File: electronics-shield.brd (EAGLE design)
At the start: 85 x 56 mm, 76 parts, among them IC1 LINEAR_MCP1703CB, J2 MICRO_USB, Q1 8 MHz, Q2 USER-SUBMITTED_MOSFET-PCHANNE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, Q3 ON-SEMICONDUCTOR---NTZD3154NT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, Q4 ON-SEMICONDUCTOR---NTZD3154NT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, U1 TLE9201SG, U2 TLE9201SG, U3 TLE9201SG, U4 TLE9201SG, U5 STM32F0XX8T, U8 EEPROM-I2C

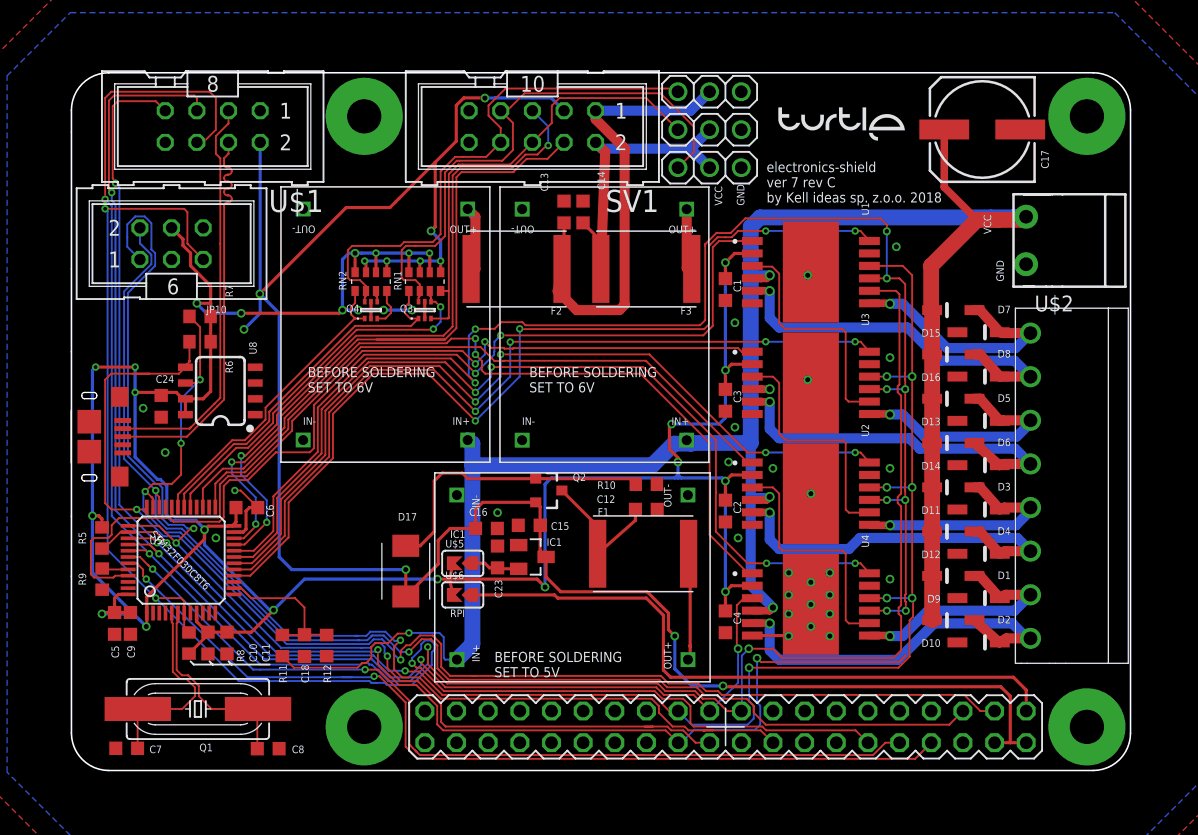
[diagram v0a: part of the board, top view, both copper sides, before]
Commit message: Thermal vias and led for checking voltages added
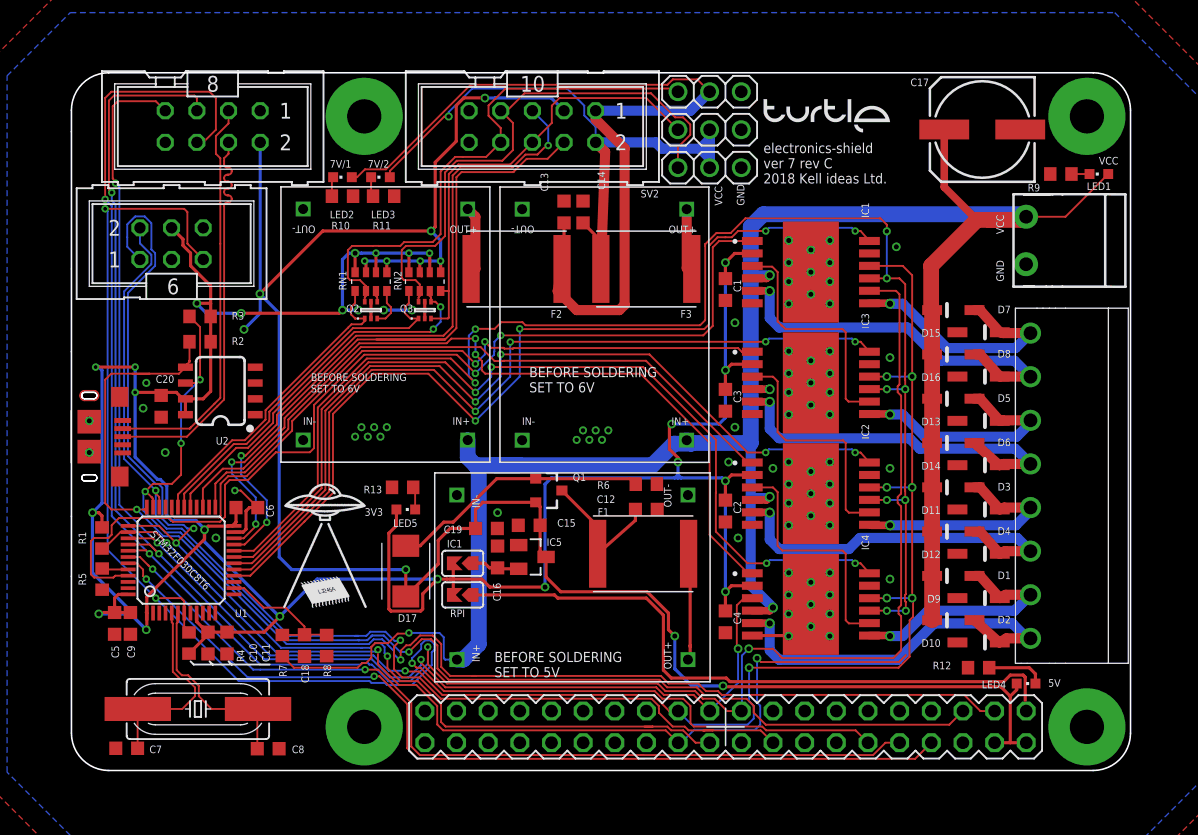
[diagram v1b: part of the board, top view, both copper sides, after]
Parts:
- removed J2: MICRO_USB, electronics-shield:MICRO_USB
- removed JP10: gniazdo IDC męskie 6pin proste, Kell Ideas:ML6
- removed JP4: Listwa kołkowa 2.54mm prosta 1x3 (3pin), Kell Ideas:1X03_ROUND_DNP
- removed JP5: Listwa stykowa 2.54mm prosta 2x20 (40-pin), wydłużona, Kell Ideas:RASPBERRY_PI_B+_CONNECTOR
- removed Q4: ON-SEMICONDUCTOR---NTZD3154NT1G_ON_SEMICONDUCTOR_NTZD3154NT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, electronics-shield:ON-SEMICONDUCTOR---NTZD3154NT1G_ON_SEMICONDUCTOR_NTZD3154NT1G_0
- removed U5: STM32F0XX8T, Kell Ideas:LQFP48
- removed U8: EEPROM-I2C, Kell Ideas:SO-08
- added $3_0_$_2018-08-14_21-12-08: Moduł przetwornicy DC-DC Step-down 4.5..28V --- regulowane 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, Kell Ideas:DC-BRICK
- added IC2: TLE9201SG, Kell Ideas:PG-DSO-12-9
- added IC5: LINEAR_MCP1703CB, electronics-shield:LINEAR_SOT23
- added J1: USB-MICRO-B, Kell Ideas:USB-MICRO-B
- added JP1: Listwa kołkowa 2.54mm prosta 1x3 (3pin), Kell Ideas:1X03_ROUND_DNP
- added LED1, LED2, LED3, LED4, LED5: LEDCHIPLED_0603, audio amplifier example:CHIPLED_0603
- added R1, R4: 10k, Kell Ideas:R0603
- added R13: 200, Kell Ideas:R0603
- added R2, R3: 4k7, Kell Ideas:R0603
- added SV2: (no value), Kell Ideas:ML10
- added Y1: 8 MHz, Kell Ideas:HC49UP
- IC1: value LINEAR_MCP1703CB -> TLE9201SG; device electronics-shield:LINEAR_SOT23 -> Kell Ideas:PG-DSO-12-9
- PCB1: value Moduł przetwornicy DC-DC Step-down 4.5..28V --- regulowane 0.8..20V MP1584 -> Listwa stykowa 2.54mm prosta 2x20 (40-pin), wydłużona; device Kell Ideas:DC-BRICK -> Kell Ideas:RASPBERRY_PI_B+_CONNECTOR
- Q1: value 8 MHz -> USER-SUBMITTED_MOSFET-PCHANNELSMD; device Kell Ideas:HC49UP -> electronics-shield:USER-SUBMITTED_SOT23-3
- Q2: value USER-SUBMITTED_MOSFET-PCHANNELSMD -> ON-SEMICONDUCTOR---NTZD3154NT1G_ON_SEMICONDUCTOR_NTZD3154NT1GON_SEMICONDUCTOR_NTZD3154NT1G_0_0; device electronics-shield:USER-SUBMITTED_SOT23-3 -> electronics-shield:ON-SEMICONDUCTOR---NTZD3154NT1G_ON_SEMICONDUCTOR_NTZD3154NT1G_0
- R10: value 100k -> 330
- R11: value 10k -> 330
- R12: value 1k -> 200
- R6: value 4k7 -> 100k
- R7: value 4k7 -> 10k
- R8: value 10k -> 1k
- R9: value 10k -> 1.5k
- SV1: value (none) -> gniazdo IDC męskie 6pin proste; device Kell Ideas:ML10 -> Kell Ideas:ML6
- U1: value TLE9201SG -> STM32F0XX8T; device Kell Ideas:PG-DSO-12-9 -> Kell Ideas:LQFP48
- U2: value TLE9201SG -> EEPROM-I2C; device Kell Ideas:PG-DSO-12-9 -> Kell Ideas:SO-08
- moved R9 83.5 mm to (79.5, 48.0), turned to 180 degrees
- moved PCB1 74.2 mm to (85.1, 56.1), turned to 180 degrees
- moved U1 55.6 mm to (8.89, 17.0), turned to 0 degrees
- moved R12 52.4 mm to (72.9, 8.38), turned to 180 degrees
- moved U2 48.1 mm to (12.0, 30.6), turned to 90 degrees
- moved R6 37.6 mm to (46.2, 23.1), turned to 180 degrees
- moved R11 37.0 mm to (25.1, 46.2), turned to 0 degrees
- moved R10 33.6 mm to (21.8, 46.2), turned to 0 degrees
- moved Q1 33.1 mm to (38.4, 22.6), turned to 270 degrees
- moved IC1 32.0 mm to (59.4, 40.1)
- moved SV1 30.4 mm to (8.13, 42.4), turned to 0 degrees
- moved R7 27.2 mm to (17.0, 10.2), turned to 270 degrees
- moved Q2 20.3 mm to (24.1, 37.1), turned to 90 degrees
- moved R8 11.1 mm to (20.6, 10.2), turned to 90 degrees
- moved JP3 6.10 mm to (51.3, 54.6)
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- renumbered C23 to C19, C24 to C20, JP9 to X2, PCB2 to $3_1_$_2018-08-14_21-12-08, PCB3 to $3_2_$_2018-08-14_21-12-08, U$1 to SV3, U$2 to X1, U$5 to SJ1, U$6 to SJ2, U3 to IC3, U4 to IC4
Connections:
- new net N$1: LED1.C, R9.1
- new net N$2: LED2.C, R10.1
- new net N$3: LED3.C, R11.1
- new net N$4: LED4.C, R12.1
- new net N$5: LED5.C, R13.1
- net +3V3: now also IC1.2, IC2.2, LED5.A, Q2.2, Q2.5, R1.2, R2.2, R3.2, R4.2, SV1.4, U1.1, U1.24, U1.48, U1.9, U2.7, U2.8; no longer JP10.4, Q4.2, Q4.5, R5.2, R6.2, R7.2, R8.2, U1.2, U2.2, U5.1, U5.24, U5.48, U5.9, U8.7, U8.8
- net +5V: now also IC5.3, LED4.A, PCB1.2, PCB1.4, Q1.2, SV2.3; no longer IC1.3, JP5.2, JP5.4, Q2.2, SV1.3
- net +5V_RAW: now also $3_0_$_2018-08-14_21-12-08.OUT1+1; no longer PCB1.OUT1+1
- net +7V/1: now also JP3.2, LED2.A, SV2.1; no longer JP4.2, SV1.1
- net +7V/2: now also JP1.2, LED3.A, SV2.2; no longer JP3.2, SV1.2
- net 3V3: now also PCB1.17; no longer JP5.17
- net 3V3_RPI: now also PCB1.1; no longer JP5.1
- net 3V3_STABILIZED: now also IC5.2; no longer IC1.2
- net 5V_NOT_TRIMMED: now also Q1.3; no longer Q2.3
- net BAT_MEAS: now also R7.1, R8.2, U1.14; no longer R11.1, R12.2, U5.14
- net BOOT0: now also R5.2, U1.44; no longer R9.2, U5.44
- net D1-R3: now also Q1.1, R6.2; no longer Q2.1, R10.2
- net DATA_N: now also J1.D-; no longer J2.D-
- net DATA_P: now also J1.D+; no longer J2.D+
- net EN1: now also IC1.12, U1.16; no longer U1.12, U5.16
- net EN2: now also U1.17; no longer U5.17
- net EN3: now also IC2.12, U1.18; no longer U2.12, U5.18
- net EN4: now also U1.19; no longer U5.19
- net GND: now also $3_0_$_2018-08-14_21-12-08.IN1-1, $3_0_$_2018-08-14_21-12-08.OUT1-1, IC1.11, IC1.13, IC1.6, IC2.11, IC2.13, IC2.6, IC5.1, J1.GND, J1.SHIELD$1, J1.SHIELD$2, J1.SHIELD$3, J1.SHIELD$4, JP1.3, PCB1.14, PCB1.20, PCB1.25, PCB1.30, PCB1.34, PCB1.39, PCB1.6, PCB1.9, R10.2, R11.2, R12.2, R13.2, R5.1, R6.1, R8.1, R9.2, SV1.3, SV2.10, SV2.9, U1.23, U1.47, U1.8, U2.2, U2.3, U2.4; no longer IC1.1, J2.GND, J2.SHIELD$1, J2.SHIELD$2, J2.SHIELD$3, J2.SHIELD$4, JP10.3, JP4.3, JP5.14, JP5.20, JP5.25, JP5.30, JP5.34, JP5.39, JP5.6, JP5.9, PCB1.IN1-1, PCB1.OUT1-1, R10.1, R12.1, R9.1, SV1.10, SV1.9, U1.11, U1.13, U1.6, U2.11, U2.13, U2.6, U5.23, U5.47, U5.8, U8.2, U8.3, U8.4
- net IN11: now also IC1.1, U1.45; no longer U1.1, U5.45
- net IN21: now also U1.32; no longer U5.32
- net IN31: now also IC2.1, U1.25; no longer U2.1, U5.25
- net IN41: now also U1.27; no longer U5.27
- net LED: now also U1.15; no longer U5.15
- net MOT11: now also IC1.5; no longer U1.5
- net MOT12: now also IC1.7; no longer U1.7
- net MOT31: now also IC2.5; no longer U2.5
- net MOT32: now also IC2.7; no longer U2.7
- net N$14: now also Q2.4, RN1.3; no longer Q4.4, RN2.3
- net N$16: now also Q2.3, RN1.4; no longer Q4.3, RN2.4
- net N$8: now also SV1.6; no longer JP10.6
- net NRST: now also PCB1.12, R4.1, SV1.5, U1.7; no longer JP10.5, JP5.12, R8.1, U5.7
- net OSCILATOR_N: now also U1.5, Y1.2; no longer Q1.2, U5.5
- net OSCILATOR_P: now also U1.6, Y1.1; no longer Q1.1, U5.6
- net RPI_CLK: now also IC1.10, IC2.10, PCB1.23, U1.39; no longer JP5.23, U1.10, U2.10, U5.39
- net RPI_MISO: now also PCB1.21, U1.40; no longer JP5.21, U5.40
- net RPI_MOSI: now also IC1.8, PCB1.19, U1.41; no longer JP5.19, U1.8, U5.41
- net RPI_RXD: now also PCB1.10, U1.42; no longer JP5.10, U5.42
- net RPI_TXD: now also PCB1.8, U1.43; no longer JP5.8, U5.43
- net SCL: now also PCB1.5, R3.1, U1.35, U2.6; no longer JP5.5, R7.1, U5.35, U8.6
- net SCL_TX: now also SV2.5, U1.21; no longer SV1.5, U5.21
- net SDA: now also PCB1.3, R2.1, U1.36, U2.5; no longer JP5.3, R6.1, U5.36, U8.5
- net SDA_RX: now also SV2.4, U1.22; no longer SV1.4, U5.22
- net SEN1: now also U1.10; no longer U5.10
- net SEN2: now also U1.11; no longer U5.11
- net SEN3: now also U1.12; no longer U5.12
- net SEN4: now also U1.13; no longer U5.13
- net SERVO1: now also JP1.1, RN2.4, SV2.6; no longer JP2.1, RN1.4, SV1.6
- net SERVO1_UC: now also RN2.3, U1.29; no longer RN1.3, U5.29
- net SERVO2: now also JP2.1, RN2.2, SV2.7; no longer JP3.1, RN1.2, SV1.7
- net SERVO2_UC: now also RN2.1, U1.30; no longer RN1.1, U5.30
- net SERVO3: now also JP3.1, Q2.6, RN1.2, SV2.8; no longer JP4.1, Q4.6, RN2.2, SV1.8
- net SERVO3_UC: now also Q2.1, RN1.1, U1.31; no longer Q4.1, RN2.1, U5.31
- net SO1-SI3: now also IC1.3; no longer U1.3
- net SO2-SI4: now also IC2.3; no longer U2.3
- net SO3-SI2: now also IC2.8; no longer U2.8
- net SPI1_NSS: now also PCB1.24, R1.1, U1.38; no longer JP5.24, R5.1, U5.38
- net SWCLK: now also PCB1.22, SV1.1, U1.37; no longer JP10.1, JP5.22, U5.37
- net SWDIO: now also PCB1.18, SV1.2, U1.34; no longer JP10.2, JP5.18, U5.34
- net TLE_NSS: now also IC1.9, IC2.9, U1.20; no longer U1.9, U2.9, U5.20
- net VCC: now also $3_0_$_2018-08-14_21-12-08.IN1+1, IC1.4, IC2.4, LED1.A, R7.2; no longer PCB1.IN1+1, R11.2, U1.4, U2.4
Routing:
- net +7V/1: track 38.0 -> 70.4 mm
- net +7V/2: track 27.1 -> 56.0 mm, vias 0 -> 1
- net +3V3: track 243.5 -> 259.2 mm
- net VCC: track 189.7 -> 199.9 mm
- net N$4: track 0.00 -> 4.70 mm
- net D1-R3: track 23.6 -> 20.9 mm
- net N$5: track 0.00 -> 1.84 mm
- net +5V: track 174.0 -> 172.3 mm
- net N$3: track 0.00 -> 1.59 mm
- net N$2: track 0.00 -> 1.57 mm
- net N$1: track 0.00 -> 1.45 mm
- net 3V3_RPI: track 51.9 -> 52.9 mm
- net BAT_MEAS: track 12.1 -> 11.2 mm
- net SERVO3_UC: track 24.9 -> 25.7 mm
- net RPI_TXD: track 74.9 -> 74.2 mm
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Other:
- board text added: "3V3"
- board text added: "5V"
- board text added: "7V/1"
- board text added: "7V/2"
- board text added: "electronics-shield ver 7 rev C 2018 Kell ideas Ltd."
- board text removed: "electronics-shield ver 7 rev C by Kell ideas sp. z.o.o. 2018"

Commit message: change few footprints, complete wiring
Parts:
- RN1, RN2: value (none) -> 1k; device electronics-shield:RESISTOR-DIL_EXB38V -> SparkFun-Resistors:0805-ARV
- moved RN2 6.12 mm to (22.4, 39.9)
- moved RN1 3.59 mm to (27.7, 39.9)
- moved Q2 1.80 mm to (22.4, 36.8)
- moved Q3 0.80 mm to (27.7, 36.8)
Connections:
- net N$14: now also RN2.3; no longer RN1.3
- net N$16: now also RN2.4; no longer RN1.4
- net SERVO1: now also RN1.4; no longer RN2.4
- net SERVO1_UC: now also RN1.3; no longer RN2.3
- net SERVO2: now also RN1.2; no longer RN2.2
- net SERVO2_UC: now also RN1.1; no longer RN2.1
- net SERVO3: now also RN2.2; no longer RN1.2
- net SERVO3_UC: now also RN2.1; no longer RN1.1
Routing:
- net +5V: track 172.3 -> 180.3 mm, vias 11 -> 12
- net SERVO3_UC: track 25.7 -> 24.3 mm
- net +3V3: track 259.2 -> 258.0 mm, vias 26 -> 22
- net SERVO1: track 36.4 -> 35.5 mm
- net SERVO2_UC: track 29.3 -> 28.6 mm
- net +7V/1: track 70.4 -> 69.7 mm
- net GND: vias 73 -> 77

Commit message: Changed microprocessor, major and minor changes
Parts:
- removed $3_0_$_2018-08-14_21-12-08, $3_1_$_2018-08-14_21-12-08, $3_2_$_2018-08-14_21-12-08: Moduł przetwornicy DC-DC Step-down 4.5..28V --- regulowane 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, Kell Ideas:DC-BRICK
- removed C10: 1u, Kell Ideas:C0603K
- removed C11, C12, C13, C14, C6, C9: 100n, Kell Ideas:C0603K
- removed C15: 4.7uF, Kell Ideas:C0603K
- removed C16: 1uF, Kell Ideas:C0603K
- removed C17: 100u, Kell Ideas:FI8_6.2
- removed C18: 22u, Kell Ideas:C0603K
- removed C5: 4u7, Kell Ideas:C0603K
- removed C7, C8: 20p, Kell Ideas:C0603K
- removed D17: SMBJ5.0A-TR, Kell Ideas:SMBJ
- removed F1, F2, F3: SL125-33, Kell Ideas:FUSC7351X125
- removed IC5: LINEAR_MCP1703CB, electronics-shield:LINEAR_SOT23
- removed Q1: USER-SUBMITTED_MOSFET-PCHANNELSMD, electronics-shield:USER-SUBMITTED_SOT23-3
- removed R1, R4, R5, R7: 10k, Kell Ideas:R0603
- removed R2, R3: 4k7, Kell Ideas:R0603
- removed R6: 100k, Kell Ideas:R0603
- removed R8: 1k, Kell Ideas:R0603
- removed SJ1, SJ2: (no value), Kell Ideas:SJ
- removed U1: STM32F0XX8T, Kell Ideas:LQFP48
- removed Y1: 8 MHz, Kell Ideas:HC49UP
- added C35, C36, C37, C38, C39: ?, Kell Ideas:C0402K
- added C40, C41: (no value), rcl:153CLV-0405
- added D20: 28V-5A, Seeed-Diode:DO-214AA
- added IC6, IC7, IC8, IC9: ACS712-LC, allegro-2:SOIC8
- added L3: ?, SparkFun-Coils:CR54
- added R22, R23, R24, R25: ?, Kell Ideas:R0402
- added U5: AOZ1284, Kell Ideas:SO-8_EXPOSED_PAD
- added U6: STM32F103VCT6, Kell Ideas:LQFP100
- C1, C19, C2, C20, C3, C4: device Kell Ideas:C0603K -> Kell Ideas:C0402K
- R10, R11, R12, R13, R9: device Kell Ideas:R0603 -> Kell Ideas:R0402
- moved C20 210.1 mm to (210.0, -26.0)
- moved LED5 186.3 mm to (207.3, -25.7), turned to 0 degrees
- moved R13 185.3 mm to (205.5, -25.9), turned to 270 degrees
- moved C19 183.5 mm to (211.1, -26.3), turned to 90 degrees
- moved Q2 146.7 mm to (83.1, -96.8), flipped to the bottom
- moved Q3 146.7 mm to (88.4, -96.8), flipped to the bottom
- moved RN1 146.7 mm to (88.4, -93.7), flipped to the bottom, turned to 180 degrees
- moved RN2 146.7 mm to (83.1, -93.7), flipped to the bottom, turned to 180 degrees
- moved U2 116.3 mm to (125.8, 6.74), flipped to the bottom, turned to 270 degrees
- moved C1 92.5 mm to (118.4, -26.3)
- moved C2 92.5 mm to (118.4, -44.1)
- moved C3 92.5 mm to (118.4, -35.2)
- moved C4 92.5 mm to (118.4, -53.0)
- moved D9 75.8 mm to (4.32, 46.2), flipped to the bottom, turned to 0 degrees
- moved D10 75.6 mm to (4.32, 42.2), flipped to the bottom, turned to 0 degrees
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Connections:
- removed net +5V_RAW: $3_0_$_2018-08-14_21-12-08.OUT1+1, F1.2
- removed net +7V/1_RAW: $3_1_$_2018-08-14_21-12-08.OUT1+1, F2.2
- removed net +7V/2_RAW: $3_2_$_2018-08-14_21-12-08.OUT1+1, F3.1
- removed net 3V3_STABILIZED: C16.1, IC5.2, SJ1.2
- removed net 5V_NOT_TRIMMED: C12.1, F1.1, Q1.3
- removed net BAT_MEAS: C18.1, R7.1, R8.2, U1.14
- removed net D1-R3: D17.A, Q1.1, R6.2
- removed net LED: U1.15
- removed net OSCILATOR_N: C7.2, U1.5, Y1.2
- removed net OSCILATOR_P: C8.2, U1.6, Y1.1
- removed net SEN1: U1.10
- removed net SEN2: U1.11
- removed net SEN3: U1.12
- removed net SEN4: U1.13
- new net BS2: C38.1, U5.2
- new net COMP: C37.1, U5.5
- new net C_COMP_R_COMP: C37.2, R25.2
- new net FB: R23.1, R24.2, U5.6
- new net FSW1: R22.2, U5.4
- new net LX: C38.2, D20.-, L3.P$1, U5.1
- new net N$10: U6.100, U6.11, U6.22, U6.28, U6.50, U6.75
- new net N$7: IC1.4, IC6.1, IC6.2
- new net N$9: U6.10, U6.19, U6.20, U6.27, U6.49, U6.74, U6.99
- new net NC: U6.73
- new net OSC_IN: U6.12
- new net OSC_OUT: U6.13
- new net PA0-WKUP: U6.23
- new net PA1: U6.24
- new net PA10: U6.69
- new net PA11: U6.70
- new net PA12: U6.71
- new net PA13: U6.72
- new net PA14: U6.76
- new net PA15: U6.77
- new net PA2: U6.25
- new net PA3: U6.26
- new net PA4: U6.29
- new net PA5: U6.30
- new net PA6: U6.31
- new net PA7: U6.32
- new net PA8: U6.67
- new net PA9: U6.68
- new net PB0: U6.35
- new net PB1: U6.36
- new net PB10: U6.47
- new net PB11: U6.48
- new net PB12: U6.51
- new net PB13: U6.52
- new net PB14: U6.53
- new net PB15: U6.54
- new net PB2: U6.37
- new net PB3: U6.89
- new net PB4: U6.90
- new net PB5: U6.91
- new net PB6: U6.92
- new net PB7: U6.93
- new net PB8: U6.95
- new net PB9: U6.96
- new net PC0: U6.15
- new net PC1: U6.16
- new net PC10: U6.78
- new net PC11: U6.79
- new net PC12: U6.80
- new net PC13-TAMPER-RTC: U6.7
- new net PC14-OSC32_IN: U6.8
- new net PC15-OSC32_OUT: U6.9
- new net PC2: U6.17
- new net PC3: U6.18
- new net PC4: U6.33
- new net PC5: U6.34
- new net PC6: U6.63
- new net PC7: U6.64
- new net PC8: U6.65
- new net PC9: U6.66
- new net PD0: U6.81
- new net PD1: U6.82
- new net PD10: U6.57
- new net PD11: U6.58
- new net PD12: U6.59
- new net PD13: U6.60
- new net PD14: U6.61
- new net PD15: U6.62
- new net PD2: U6.83
- new net PD3: U6.84
- new net PD4: U6.85
- new net PD5: U6.86
- new net PD6: U6.87
- new net PD7: U6.88
- new net PD8: U6.55
- new net PD9: U6.56
- new net PE0: U6.97
- new net PE1: U6.98
- new net PE10: U6.41
- new net PE11: U6.42
- new net PE12: U6.43
- new net PE13: U6.44
- new net PE14: U6.45
- new net PE15: U6.46
- new net PE2: U6.1
- new net PE3: U6.2
- new net PE4: U6.3
- new net PE5: U6.4
- new net PE6: U6.5
- new net PE7: U6.38
- new net PE8: U6.39
- new net PE9: U6.40
- new net SS1: C39.2, U5.7
- new net VBAT: U6.6
- new net VREF+: U6.21
- net +3V3: no longer C10.1, C11.1, C5.1, C6.1, C9.1, R1.2, R2.2, R3.2, R4.2, SJ1.1, SJ2.1, U1.1, U1.24, U1.48, U1.9
- net +5V: now also C35.1, C40.+, L3.P$2, R23.2; no longer C15.1, D17.C, IC5.3, Q1.2
- net +7V/1: no longer C13.1, F2.1
- net +7V/2: no longer C14.1, F3.2
- net 3V3_RPI: no longer SJ2.2
- net BOOT0: now also U6.94; no longer R5.2, U1.44
- net EN1: no longer U1.16
- net EN2: no longer U1.17
- net EN3: no longer U1.18
- net EN4: no longer U1.19
- net GND: now also C35.2, C36.2, C39.1, C40.-, C41.-, D20.+, IC6.5, IC7.5, IC8.5, IC9.5, R22.1, R24.1, R25.1, U5.3; no longer $3_0_$_2018-08-14_21-12-08.IN1-1, $3_0_$_2018-08-14_21-12-08.OUT1-1, $3_1_$_2018-08-14_21-12-08.IN1-1, $3_1_$_2018-08-14_21-12-08.OUT1-1, $3_2_$_2018-08-14_21-12-08.IN1-1, $3_2_$_2018-08-14_21-12-08.OUT1-1, C10.2, C11.2, C12.2, C13.2, C14.2, C15.2, C16.2, C17.-, C18.2, C5.2, C6.2, C7.1, C8.1, C9.2, IC5.1, R5.1, R6.1, R8.1, U1.23, U1.47, U1.8
- net IN11: no longer U1.45
- net IN21: no longer U1.32
- net IN31: no longer U1.25
- net IN41: no longer U1.27
- net MOT11: now also X2.8; no longer X2.7
- net MOT12: now also X2.7; no longer X2.8
- net MOT21: now also X2.6; no longer X2.5
- net MOT22: now also X2.5; no longer X2.6
- net MOT31: now also X2.4; no longer X2.3
- net MOT32: now also X2.3; no longer X2.4
- net MOT41: now also X2.2; no longer X2.1
- net MOT42: now also X2.1; no longer X2.2
- net NRST: now also U6.14; no longer R4.1, U1.7
- net RPI_CLK: no longer U1.39
- net RPI_MISO: no longer U1.40
- net RPI_MOSI: no longer U1.41
- net RPI_RXD: no longer U1.42
- net RPI_TXD: no longer U1.43
- net SCL: no longer R3.1, U1.35
- net SCL_TX: no longer U1.21
- net SDA: no longer R2.1, U1.36
- net SDA_RX: no longer U1.22
- net SERVO1_UC: no longer U1.29
- net SERVO2_UC: no longer U1.30
- net SERVO3_UC: no longer U1.31
- net SPI1_NSS: no longer R1.1, U1.38
- net SWCLK: no longer U1.37
- net SWDIO: no longer U1.34
- net TLE_NSS: no longer U1.20
- net VCC: now also C36.1, C41.+, IC6.3, IC6.4, IC6.8, IC7.8, IC8.8, IC9.8, U5.P$1; no longer $3_0_$_2018-08-14_21-12-08.IN1+1, $3_1_$_2018-08-14_21-12-08.IN1+1, $3_2_$_2018-08-14_21-12-08.IN1+1, C17.+, IC1.4, R7.2
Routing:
- net +3V3: track 258.0 -> 0.00 mm, vias 22 -> 0
- net +5V: track 180.3 -> 0.00 mm, vias 12 -> 0
- net RPI_MOSI: track 160.1 -> 0.00 mm, vias 4 -> 0
- net RPI_CLK: track 160.1 -> 0.00 mm, vias 10 -> 0
- net NRST: track 120.0 -> 0.00 mm, vias 3 -> 0
- net TLE_NSS: track 118.1 -> 0.00 mm, vias 10 -> 0
- net RPI_MISO: track 111.1 -> 0.00 mm, vias 4 -> 0
- net SDA: track 104.0 -> 0.00 mm, vias 2 -> 0
- net GND: track 9.94 -> 108.9 mm, vias 77 -> 48
- net SCL: track 97.9 -> 0.00 mm, vias 4 -> 0
- net SWCLK: track 93.1 -> 0.00 mm, vias 3 -> 0
- net VCC: track 199.9 -> 107.6 mm, vias 5 -> 0
- net SWDIO: track 88.0 -> 0.00 mm, vias 2 -> 0
- net SPI1_NSS: track 80.4 -> 0.00 mm, vias 3 -> 0
- net IN11: track 78.6 -> 0.00 mm, vias 2 -> 0
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- removed copper zone on layer 1, net GND
- removed copper zone on layer 16, net GND
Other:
- board text added: "electronics-shield ver 8 2018 Kell ideas Ltd."
- board text removed: "BEFORE SOLDERING SET TO 6V"
- board text removed: "electronics-shield ver 7 rev C 2018 Kell ideas Ltd."
